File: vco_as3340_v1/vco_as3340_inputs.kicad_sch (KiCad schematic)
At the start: 36 parts, among them J100 FREQ_CV, J101 SYNC

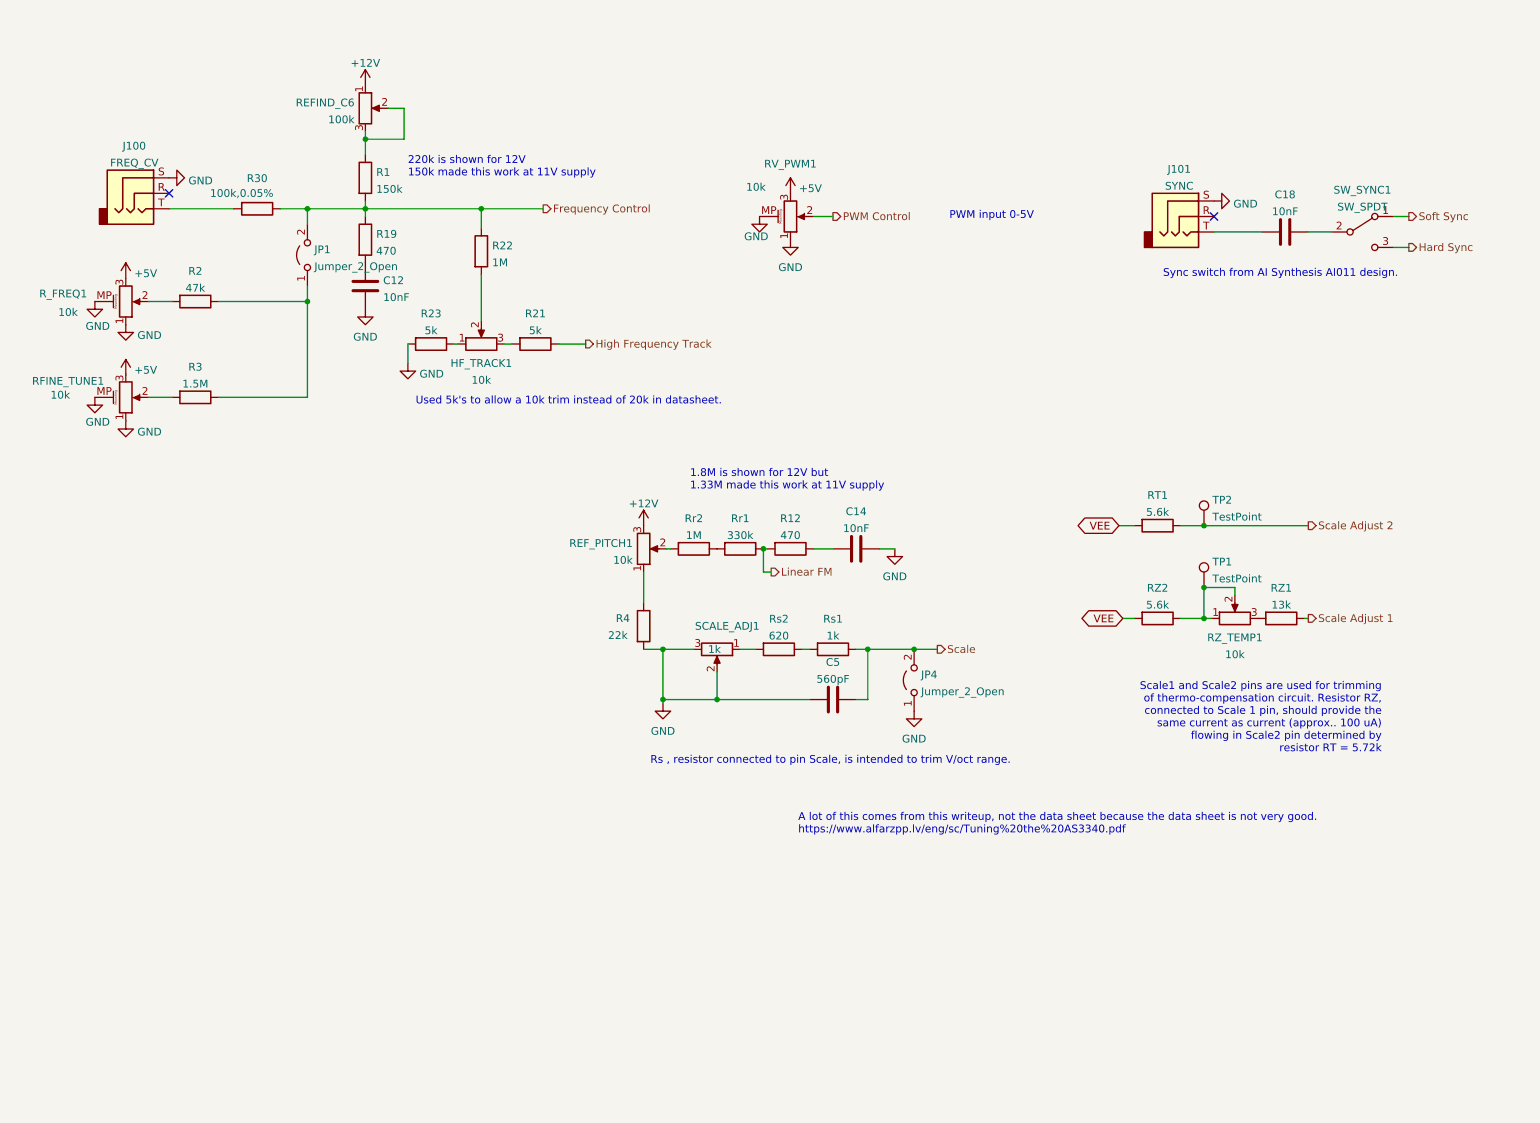
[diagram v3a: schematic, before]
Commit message: Schematic Changes v1 to v2
 - R10 = 47k
 - R9 = 0ohm
 - New C1 100pF across R10 and R9
 - New C15 10uF polarized cap from -5 to GND.
 - R6 DNU
 - R21 & R23 changed to 5.1k
 - RZ1 changed to 18k
 - R26 changed to 100k and new R31 is 100k.
 - New  R32 for 'hysteresis' between PWM and Pulse.
 - Separated grounds on Linear FM and Scale Adj. Circuits for clarity.
 - Added another TL072 (U6) and supporting circuits.
    - This is intended to supply two reference voltages from the 5V
source.
    - The idea is to provide Soft Sync (pin 9) with a stable voltage
of 1/3*Supply, which is something like 11.3/3.
    - The other REF_PITCH2 is for the Linear FM circuit. Some resistors
probably aren't right for this yet, and I think it can completely
replace REF_PITCH pot so I've placed a jumper there to allow either if
it doesn't work out.
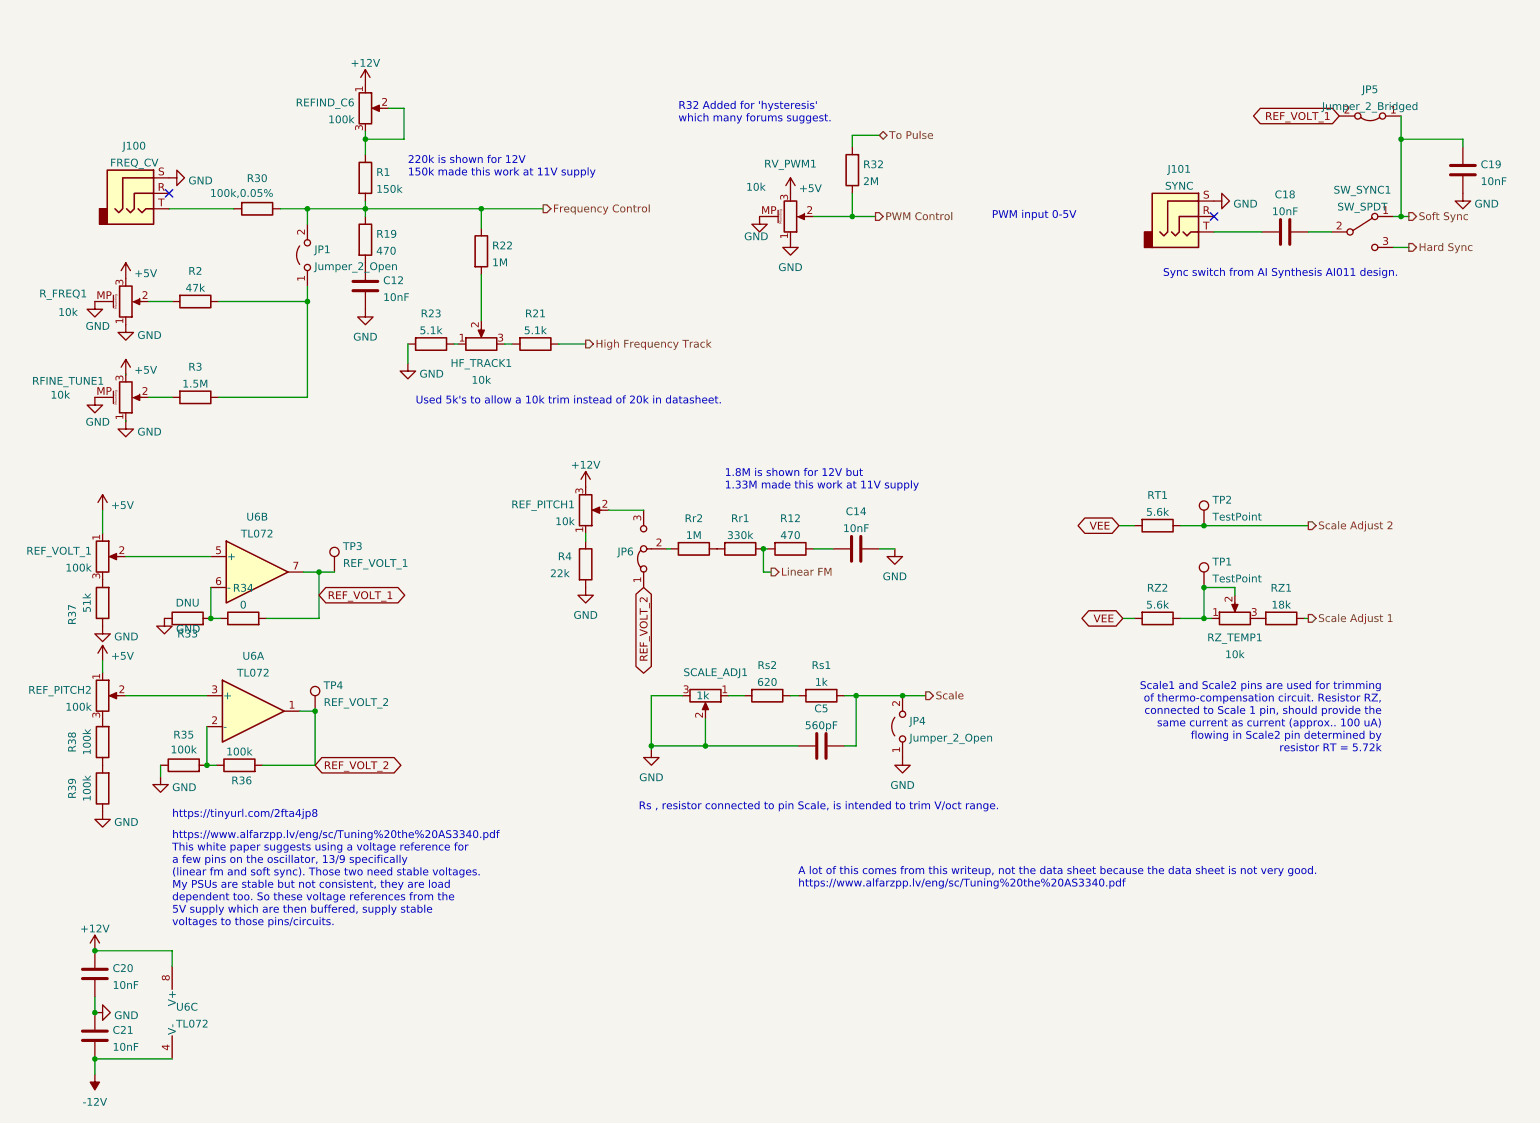
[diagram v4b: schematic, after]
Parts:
- added C19, C20, C21: 10nF, Capacitor_SMD:C_1206_3216Metric_Pad1.33x1.80mm_HandSolder, symbol Device:C
- added JP5: Jumper_2_Bridged, Jumper:SolderJumper-2_P1.3mm_Bridged_Pad1.0x1.5mm, symbol Jumper:Jumper_2_Bridged
- added JP6: Jumper_3_Bridged12, Jumper:SolderJumper-3_P1.3mm_Bridged12_Pad1.0x1.5mm, symbol Jumper:Jumper_3_Bridged12
- added R32: 2M, Resistor_SMD:R_1206_3216Metric_Pad1.30x1.75mm_HandSolder, symbol Device:R
- added R33: DNU, Resistor_SMD:R_1206_3216Metric_Pad1.30x1.75mm_HandSolder, symbol Device:R
- added R34: 0, Resistor_SMD:R_1206_3216Metric_Pad1.30x1.75mm_HandSolder, symbol Device:R
- added R35, R36, R38, R39: 100k, Resistor_SMD:R_1206_3216Metric_Pad1.30x1.75mm_HandSolder, symbol Device:R
- added R37: 51k, Resistor_SMD:R_1206_3216Metric_Pad1.30x1.75mm_HandSolder, symbol Device:R
- added REF_PITCH2, REF_VOLT_1: 100k, Potentiometer_THT:Potentiometer_Bourns_3296W_Vertical, symbol Device:R_Potentiometer
- added TP3: REF_VOLT_1, Connector_PinHeader_2.54mm:PinHeader_1x01_P2.54mm_Vertical, symbol Connector:TestPoint
- added TP4: REF_VOLT_2, Connector_PinHeader_2.54mm:PinHeader_1x01_P2.54mm_Vertical, symbol Connector:TestPoint
- added U6: TL072, Package_DIP:DIP-8_W7.62mm_Socket_LongPads, symbol Amplifier_Operational:TL072
- R21, R23: value 5k -> 5.1k
- RZ1: value 13k -> 18k
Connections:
- net +12V: now also C20.1, U6.8 (V+)
- net +5V: now also REF_PITCH2.1, REF_VOLT_1.1
- net GND: now also C19.1, C20.2, C21.1, R33.1, R35.1, R37.1, R39.1
- net PWM Control: now also R32.1
- net Soft Sync: now also C19.2, JP5.1 (A)
- net at Rr2.2: now also JP6.2 (C); no longer REF_PITCH1.2
- new net: R35.2, R36.1, U6.2 (-)
- new net: REF_PITCH2.2, U6.3 (+)
- new net: R37.2, REF_VOLT_1.3
- new net: JP6.3 (B), REF_PITCH1.2
- new net: R38.2, REF_PITCH2.3
- new net: R38.1, R39.2
- new net: REF_VOLT_1.2, U6.5 (+)
- new net: R33.2, R34.1, U6.6 (-)
- new net -12V: C21.2, U6.4 (V-)
- new net REF_VOLT_1: JP5.2 (B), R34.2, TP3.1, U6.7
- new net REF_VOLT_2: JP6.1 (A), R36.2, TP4.1, U6.1
- new net To Pulse: R32.2
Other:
- note added: "R32 Added for 'hysteresis' which many forums suggest."
- note added: "https://tinyurl.com/2fta4jp8"
- note added: "https://www.alfarzpp.lv/eng/sc/Tuning%20the%20AS3340.pdf This white paper suggests using a voltage reference for a few pins on the oscillator, 13/9 specifically (linear fm and soft sync). Those two need stable voltages. My PSUs are stable but not consistent, they are load dependent too. So these voltage references from the 5V supply which are then buffered, supply stable voltages to those pins/ci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"
- moved on the sheet: C5, JP4, R4, REF_PITCH1, Rs1, Rs2, SCALE_ADJ1

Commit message: v2 re-layout pcb
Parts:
- removed JP1: Jumper_2_Open, Connector_PinHeader_2.54mm:PinHeader_1x02_P2.54mm_Vertical, symbol Jumper:Jumper_2_Open
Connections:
- net +12V: now also REF_PITCH1.1; no longer REF_PITCH1.3
- net Frequency Control: now also R2.1, R3.1
- net at R4.1: now also REF_PITCH1.3; no longer REF_PITCH1.1
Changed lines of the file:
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@@
   (title_block
     (title "3340_VCO")
-    (date "2022-07-02")
-    (rev "1.0")
+    (date "2022-12-09")
+    (rev "2.0")
     (company "RobotDialogs")
   )
@@
     (stroke (width 0) (type default) (color 0 0 0 0))
   )
-  (wire (pts (xy 60.325 59.69) (xy 60.325 62.23))
-    (stroke (width 0) (type default) (color 0 0 0 0))
-  )
   (wire (pts (xy 125.73 135.255) (xy 140.97 135.255))
     (stroke (width 0) (type default) (color 0 0 0 0))
@@
     (stroke (width 0) (type default) (color 0 0 0 0))
   )
-  (wire (pts (xy 60.325 46.99) (xy 60.325 49.53))
-    (stroke (width 0) (type default) (color 0 0 0 0))
-  )
   (wire (pts (xy 26.67 96.52) (xy 26.67 100.33))
     (stroke (width 0) (type default) (color 0 0 0 0))
@@
   )
   (wire (pts (xy 209.296 50.8) (xy 217.17 50.8))
+    (stroke (width 0) (type default) (color 0 0 0 0))
+  )
+  (wire (pts (xy 60.325 46.99) (xy 60.325 62.23))
     (stroke (width 0) (type default) (color 0 0 0 0))
   )
@@
     (pin "3")
   )
-  (symbol (lib_id "Device:R_Potentiometer") (at 106.045 96.52 0) (mirror x) (unit 1)
-    (in_bom yes) (on_board yes) (fields_autoplaced)
-    (property "Reference" "REF_PITCH1" (id 0) (at 104.2671 95.6115 0)
-      (effects (font (size 1.27 1.27)) (justify right))
-    )
-    (property "Value" "10k" (id 1) (at 104.2671 98.3866 0)
+  (symbol (lib_id "Device:R_Potentiometer") (at 106.045 96.52 0) (unit 1)
+    (in_bom yes) (on_board yes) (fields_autoplaced)
+    (property "Reference" "REF_PITCH1" (id 0) (at 104.267 95.6115 0)
+      (effects (font (size 1.27 1.27)) (justify right))
+    )
+    (property "Value" "10k" (id 1) (at 104.267 98.3866 0)
       (effects (font (size 1.27 1.27)) (justify right))
     )
@@
     (pin "1")
   )
-  (symbol (lib_id "Jumper:Jumper_2_Open") (at 60.325 54.61 90) (unit 1)
-    (in_bom yes) (on_board yes) (fields_autoplaced)
-    (property "Reference" "JP1" (id 0) (at 61.468 53.7015 90)
-      (effects (font (size 1.27 1.27)) (justify right))
-    )
-    (property "Value" "Jumper_2_Open" (id 1) (at 61.468 56.4766 90)
-      (effects (font (size 1.27 1.27)) (justify right))
-    )
-    (property "Footprint" "Connector_PinHeader_2.54mm:PinHeader_1x02_P2.54mm_Vertical" (id 2) (at 60.325 54.61 0)
-      (effects (font (size 1.27 1.27)) hide)
-    )
-    (property "Datasheet" "~" (id 3) (at 60.325 54.61 0)
-      (effects (font (size 1.27 1.27)) hide)
-    )
-    (pin "1")
-    (pin "2")
-  )
   (symbol (lib_id "power:GND") (at 36.195 140.335 0) (mirror y) (unit 1)

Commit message: Routing done
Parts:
- removed JP6: Jumper_3_Bridged12, Jumper:SolderJumper-3_P1.3mm_Bridged12_Pad1.0x1.5mm, symbol Jumper:Jumper_3_Bridged12
- removed REF_PITCH1: 10k, Potentiometer_THT:Potentiometer_Bourns_3296W_Vertical, symbol Device:R_Potentiometer
- added J1: FREQ_CV2, My Stuff:Jack_3.5mm_MJ-355W_Vertical, symbol Connector:AudioJack3
- added R5: 100k,0.05%, Resistor_SMD:R_1206_3216Metric_Pad1.30x1.75mm_HandSolder, symbol Device:R
- R4: value 22k -> 0
- TP4: value REF_VOLT_2 -> REF_PITCH_1
- renumbered REF_PITCH2 to REF_PITCH1
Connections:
- net REF_VOLT_2 is gone; now on net REF_PITCH1: R36.2, TP4.1, U6.1
- net +5V: now also R4.2; no longer REF_VOLT_1.1
- net Frequency Control: now also R5.1
- net GND: now also J1.S; no longer R4.2
- net REF_PITCH1: now reaches Rr2.2
- net at R4.1: now also REF_VOLT_1.1
- new net: J1.T, R5.2
- no-connect marks 2 -> 3
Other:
- note added: "https://www.alfarzpp.lv/eng/sc/Tuning%20the%20AS3340.pdf This white paper suggests using a voltage reference for a few pins on the oscillator, pins 13/9 specifically (linear fm and soft sync). Those two need stable voltages. My PSUs are stable but not consistent, they are load dependent too. So these voltage references from the 5V supply which are then buffered, supply stable voltages to those pi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"
- note removed: "https://www.alfarzpp.lv/eng/sc/Tuning%20the%20AS3340.pdf This white paper suggests using a voltage reference for a few pins on the oscillator, 13/9 specifically (linear fm and soft sync). Those two need stable voltages. My PSUs are stable but not consistent, they are load dependent too. So these voltage references from the 5V supply which are then buffered, supply stable voltages to those pins/ci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"

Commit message: Changes to v2 from testing
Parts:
- removed C19: 10nF, Capacitor_SMD:C_1206_3216Metric_Pad1.33x1.80mm_HandSolder, symbol Device:C
- added JP1: Jumper_2_Open, Jumper:SolderJumper-2_P1.3mm_Open_Pad1.0x1.5mm, symbol Jumper:Jumper_2_Open
- added R40: 2.5k, Resistor_SMD:R_1206_3216Metric_Pad1.30x1.75mm_HandSolder, symbol Device:R
- added R41: 0, Resistor_SMD:R_1206_3216Metric_Pad1.30x1.75mm_HandSolder, symbol Device:R
- R21: value 5.1k -> 10k
- R23: value 5.1k -> 0
- R33: value DNU -> 100k
- R34, R4: value 0 -> 100k
- Rr1: value 330k -> 220k
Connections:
- net +12V: no longer REFIND_C6.1
- net +5V: now also R40.2; no longer RV_PWM1.3
- net GND: now also R41.1; no longer RV_PWM1.1
- net REF_PITCH1: now also REFIND_C6.1
- net Soft Sync: now also JP1.2 (B); no longer SW_SYNC1.1 (A)
- net VEE renamed -5V
- new net: JP1.1 (A), SW_SYNC1.1 (A)
- new net: R40.1, RV_PWM1.3
- new net: R41.2, RV_PWM1.1
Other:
- note added: "1.8M is shown for 12V but 1.33M made this work at 11V supply 1.22M worked for REV_PITCH1=9.7V"
- note added: "20k trim pot in datasheet."
- note added: "PWM input 0-5V (4V is 100% though)."
- note added: "REF_PITCH1 here improved frequency stability vs supply (Vcc) changes significantly."
- note added: "Sync switch from AI Synthesis AI011 design. Only makes sense to include switch if JP5 is open."
- note added: "Want 1/3 Vcc (~3.75V)"
- note added: "~9.7V is a good starting point."
- note removed: "1.8M is shown for 12V but 1.33M made this work at 11V supply"
- note removed: "PWM input 0-5V"
- note removed: "Sync switch from AI Synthesis AI011 design."
- note removed: "Used 5k's to allow a 10k trim instead of 20k in datasheet."
- moved on the sheet: RT1, RZ1, RZ2, RZ_TEMP1, TP1, TP2

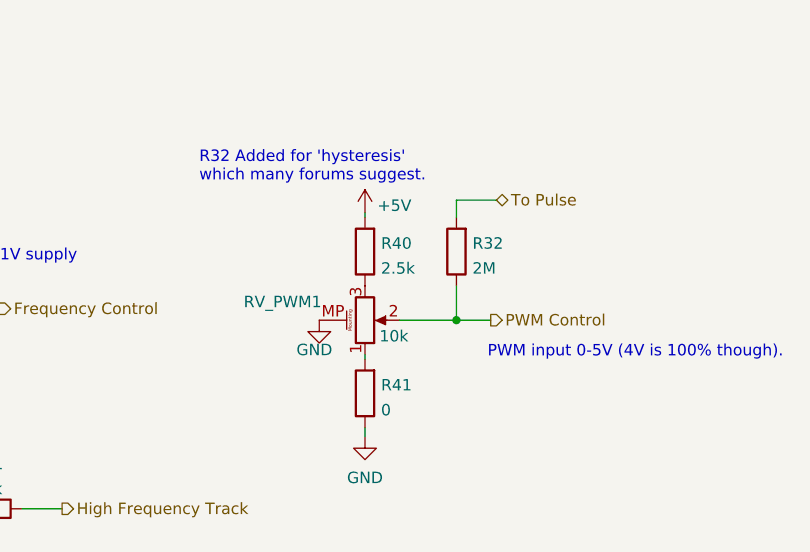
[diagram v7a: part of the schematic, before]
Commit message: Add v2.1 schematic pdf
Adjusted R40 to be 2.4k instead of 2.5k which isn't an E24 value.
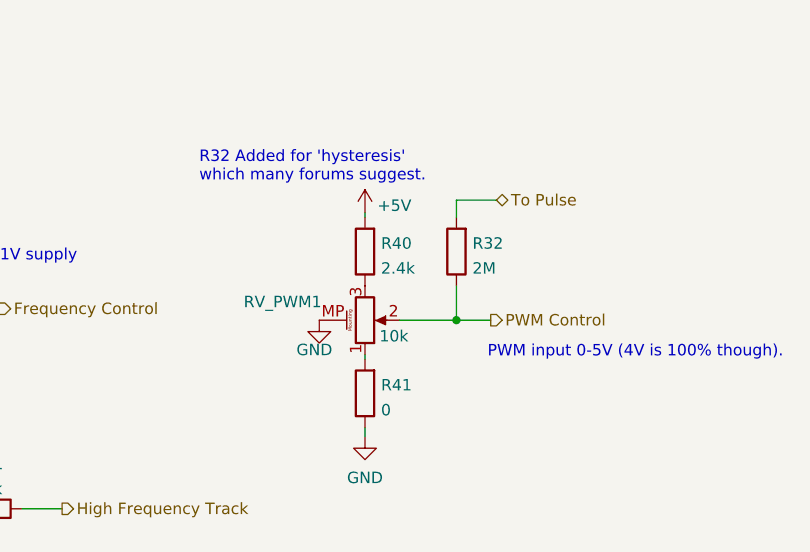
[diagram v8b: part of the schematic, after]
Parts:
- R40: value 2.5k -> 2.4k
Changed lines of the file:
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@@
       (effects (font (size 1.27 1.27)) (justify right))
     )
-    (property "Value" "2.5k" (id 1) (at 141.478 42.5066 0)
+    (property "Value" "2.4k" (id 1) (at 141.478 42.5066 0)
       (effects (font (size 1.27 1.27)) (justify right))
     )
